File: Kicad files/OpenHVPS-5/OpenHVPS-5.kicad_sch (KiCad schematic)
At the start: 86 parts, among them J1 Conn_01x03_Male, Q1 FQT7N10, Q2 BC846A, Q3 MMBT3906, Q4 MMBT3906, U1 MAX6008AEUR+T, U2 74HC14, U3 MAX4162, U4 CD14538BM

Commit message: Updated ground plane changed, capacitor to 47uF
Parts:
- C4: value 100uF -> 47uF
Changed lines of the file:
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@@
   (title_block
     (title "SafePulse")
-    (date "2021-02-20")
+    (date "2021-02-21")
     (rev "1.12")
     (company "SafeCast Team")
@@
       (effects (font (size 1.27 1.27)) (justify left))
     )
-    (property "Value" "100uF" (id 1) (at 105.791 28.448 0)
+    (property "Value" "47uF" (id 1) (at 105.791 28.448 0)
       (effects (font (size 1.27 1.27)) (justify left))
     )
@@
       (effects (font (size 1.27 1.27)) hide)
     )
-    (property "Datasheet" "https://www.digikey.com/en/products/detail/cal-chip-electronics-inc/GMC21X5R107M6R3NT/12140431" (id 3) (at 102.87 27.305 0)
+    (property "Datasheet" "https://www.digikey.com/en/products/detail/taiyo-yuden/EMK316BBJ476ML-T/7067010" (id 3) (at 102.87 27.305 0)
       (effects (font (size 1.27 1.27)) hide)
     )
@@
       (effects (font (size 1.27 1.27)) hide)
     )
-    (property "Datasheet" "https://www.digikey.com/en/products/detail/bourns-inc/MH2029-221Y/3767626" (id 3) (at 81.28 28.575 0)
+    (property "Datasheet" "https://www.digikey.com/en/products/detail/tdk-corporation/MPZ2012S331ATD25/5040330" (id 3) (at 81.28 28.575 0)
       (effects (font (size 1.27 1.27)) hide)
     )
@@
       (effects (font (size 1.27 1.27)) hide)
     )
-    (property "Datasheet" "https://www.digikey.com/en/products/detail/bourns-inc/MH2029-221Y/3767626" (id 3) (at 115.57 29.845 0)
+    (property "Datasheet" "https://www.digikey.com/en/products/detail/tdk-corporation/MPZ2012S331ATD25/5040330" (id 3) (at 115.57 29.845 0)
       (effects (font (size 1.27 1.27)) hide)
     )
@@
     )
     (path "/00000000-0000-0000-0000-000060023647"
-      (reference "C4") (unit 1) (value "100uF") (footprint "Capacitor_SMD:C_1210_3225Metric")
+      (reference "C4") (unit 1) (value "47uF") (footprint "Capacitor_SMD:C_1210_3225Metric")
     )
     (path "/00000000-0000-0000-0000-0000600248db"

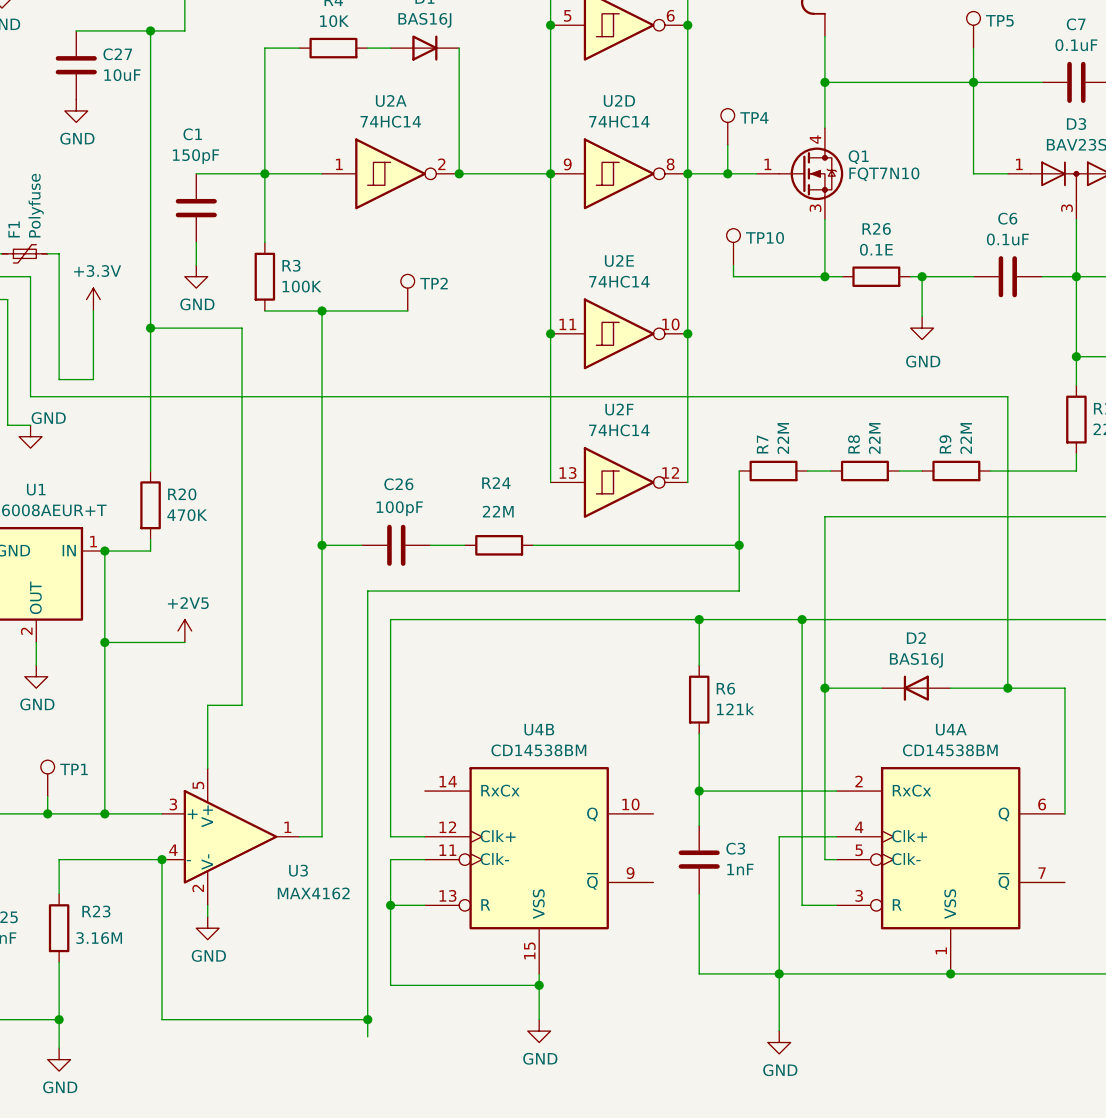
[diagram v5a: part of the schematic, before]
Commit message: added digikey bom from Allan and move U4 label
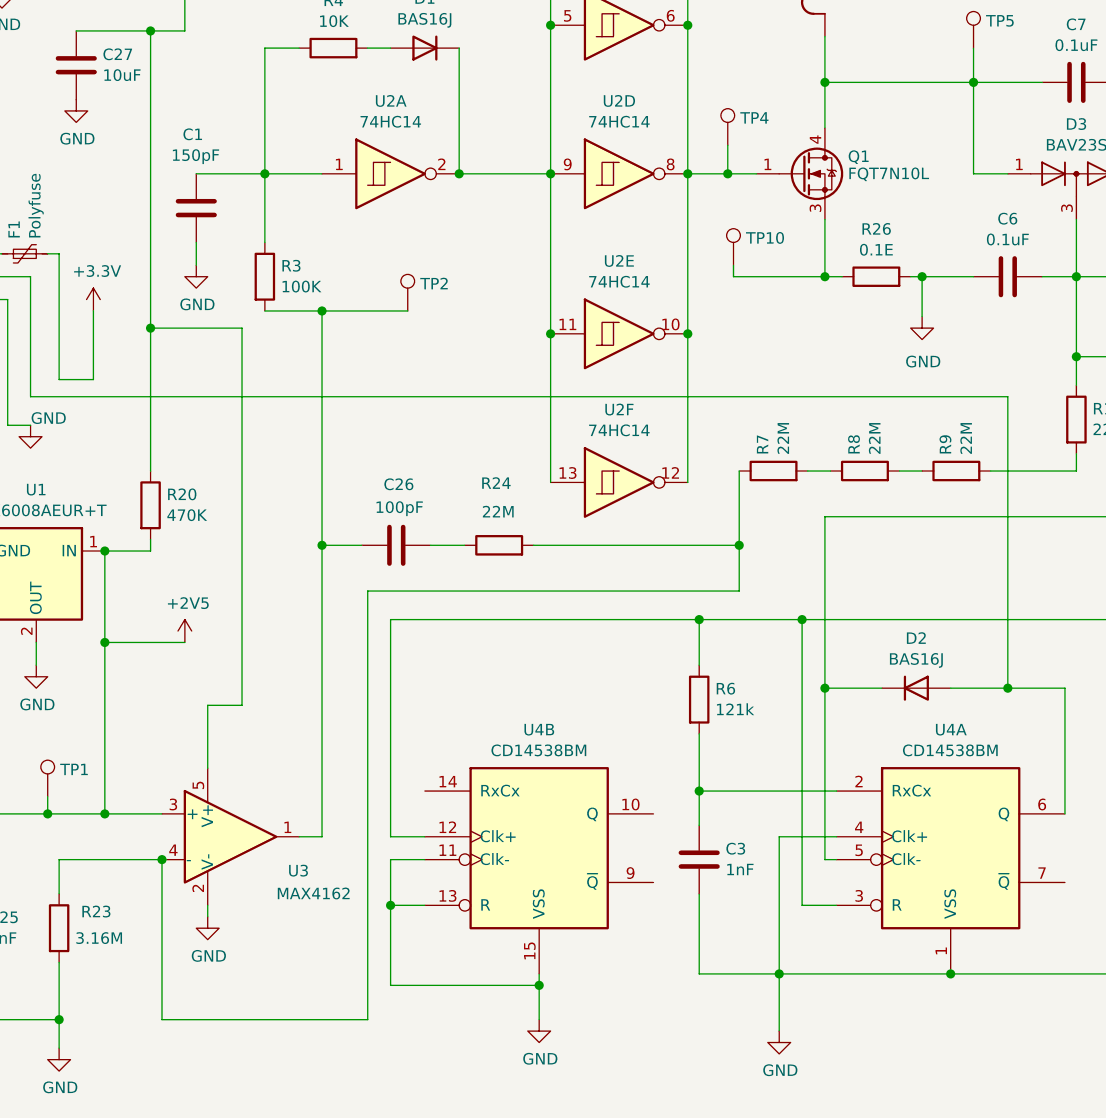
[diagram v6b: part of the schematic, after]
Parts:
- Q1: value FQT7N10 -> FQT7N10L
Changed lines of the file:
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@@
   (title_block
     (title "SafePulse")
-    (date "2021-02-21")
+    (date "2021-02-24")
     (rev "1.12")
     (company "SafeCast Team")
@@
   (junction (at 59.69 103.505) (diameter 1.016) (color 0 0 0 0))
   (junction (at 59.69 129.54) (diameter 1.016) (color 0 0 0 0))
-  (junction (at 64.77 182.245) (diameter 1.016) (color 0 0 0 0))
   (junction (at 67.31 169.545) (diameter 1.016) (color 0 0 0 0))
   (junction (at 74.93 88.265) (diameter 1.016) (color 0 0 0 0))
@@
     (stroke (width 0) (type solid) (color 0 0 0 0))
   )
+  (wire (pts (xy 41.91 182.245) (xy 64.77 182.245))
+    (stroke (width 0) (type solid) (color 0 0 0 0))
+  )
   (wire (pts (xy 44.45 72.39) (xy 44.45 62.23))
     (stroke (width 0) (type solid) (color 0 0 0 0))
@@
     (stroke (width 0) (type solid) (color 0 0 0 0))
   )
-  (wire (pts (xy 64.77 134.62) (xy 64.77 182.245))
-    (stroke (width 0) (type solid) (color 0 0 0 0))
-  )
   (wire (pts (xy 64.77 134.62) (xy 106.045 134.62))
     (stroke (width 0) (type solid) (color 0 0 0 0))
   )
-  (wire (pts (xy 64.77 182.245) (xy 41.91 182.245))
-    (stroke (width 0) (type solid) (color 0 0 0 0))
-  )
-  (wire (pts (xy 64.77 182.245) (xy 64.77 184.15))
+  (wire (pts (xy 64.77 182.245) (xy 64.77 134.62))
     (stroke (width 0) (type solid) (color 0 0 0 0))
   )
@@
       (effects (font (size 1.27 1.27)) (justify left) hide)
     )
-    (property "Datasheet" "https://www.digikey.com/en/products/detail/murata-electronics/PRG21BC0R2MM1RA/966726" (id 3) (at 26.67 97.155 0)
+    (property "Datasheet" "https://www.digikey.com/en/products/detail/murata-electronics/PRG21BC0R6MM1RA/2595395?s=N4IgTCBcDaICwE4AMBaAHAVgIyqygcgCIgC6AvkA" (id 3) (at 26.67 97.155 0)
       (effects (font (size 1.27 1.27)) hide)
     )
@@
       (effects (font (size 1.27 1.27)) hide)
     )
-    (property "Datasheet" "https://www.digikey.com/en/products/detail/panasonic-electronic-components/ERJ-6ENF2002V/111532" (id 3) (at 263.525 144.145 0)
+    (property "Datasheet" "https://www.digikey.com/en/products/detail/stackpole-electronics-inc/RMCF0805FT20K0/1760314" (id 3) (at 263.525 144.145 0)
       (effects (font (size 1.27 1.27)) hide)
     )
@@
       (effects (font (size 1.27 1.27)) (justify left))
     )
-    (property "Value" "FQT7N10" (id 1) (at 118.11 88.265 0)
+    (property "Value" "FQT7N10L" (id 1) (at 118.11 88.265 0)
       (effects (font (size 1.27 1.27)) (justify left))
     )
@@
       (effects (font (size 1.27 1.27) italic) hide)
     )
-    (property "Datasheet" "https://www.infineon.com/dgdl/irf6655pbf.pdf?fileId=5546d462533600a4015355ec76961a5b" (id 3) (at 113.03 88.265 0)
+    (property "Datasheet" "https://www.digikey.com/en/products/detail/on-semiconductor/FQT7N10LTF/965354" (id 3) (at 113.03 88.265 0)
       (effects (font (size 1.27 1.27)) (justify left) hide)
     )
@@
       (effects (font (size 1.27 1.27)) (justify left) hide)
     )
-    (property "Datasheet" "https://www.digikey.com/en/products/detail/maxim-integrated/MAX4162EUK-T/470825" (id 3) (at 49.53 156.845 0)
+    (property "Datasheet" "https://www.digikey.com/en/products/detail/maxim-integrated/MAX4162EUK-T/774077" (id 3) (at 49.53 156.845 0)
       (effects (font (size 1.27 1.27)) hide)
     )
@@
     )
     (path "/0b3e807e-2e2e-4d01-9bff-0d612d23cbec"
-      (reference "Q1") (unit 1) (value "FQT7N10") (footprint "Package_TO_SOT_SMD:SOT-223-3_TabPin4")
+      (reference "Q1") (unit 1) (value "FQT7N10L") (footprint "Package_TO_SOT_SMD:SOT-223-3_TabPin4")
     )
     (path "/00000000-0000-0000-0000-000060126f57"

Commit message: Test
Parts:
- C1: manf# (none) -> test
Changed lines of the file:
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@@
+      (effects (font (size 1.27 1.27)) hide)
+    )
+    (property "manf#" "test" (id 4) (at 45.72 92.075 0)
       (effects (font (size 1.27 1.27)) hide)
     )

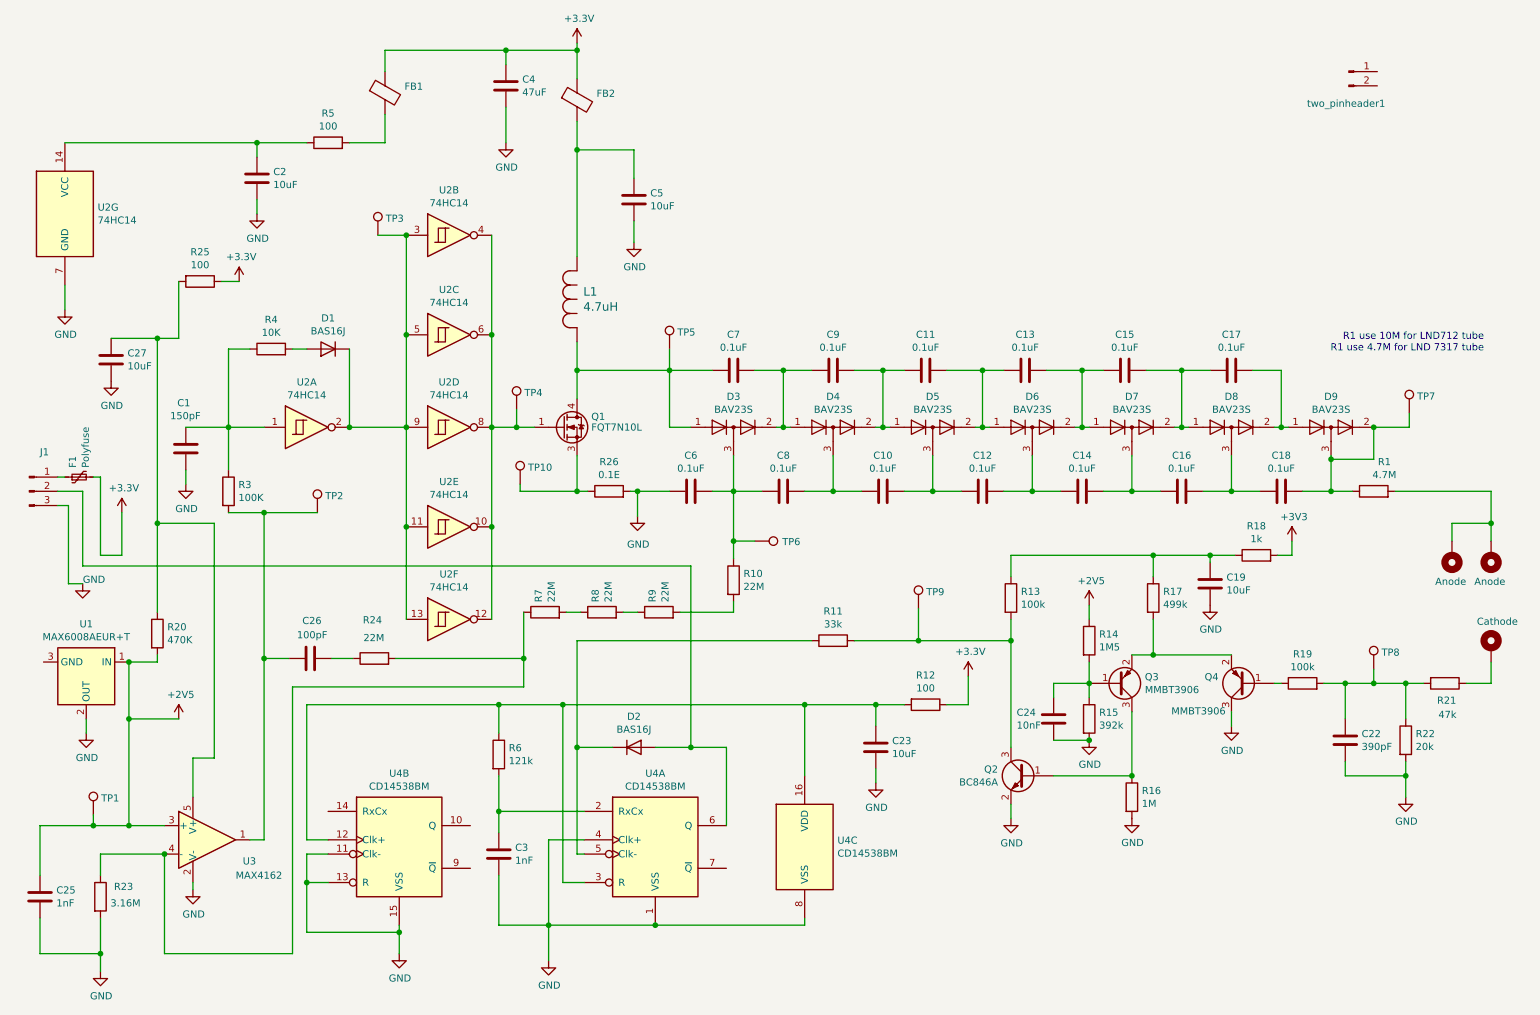
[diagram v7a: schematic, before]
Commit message: Cahged pin sof U3 Max4162. V1.20.0
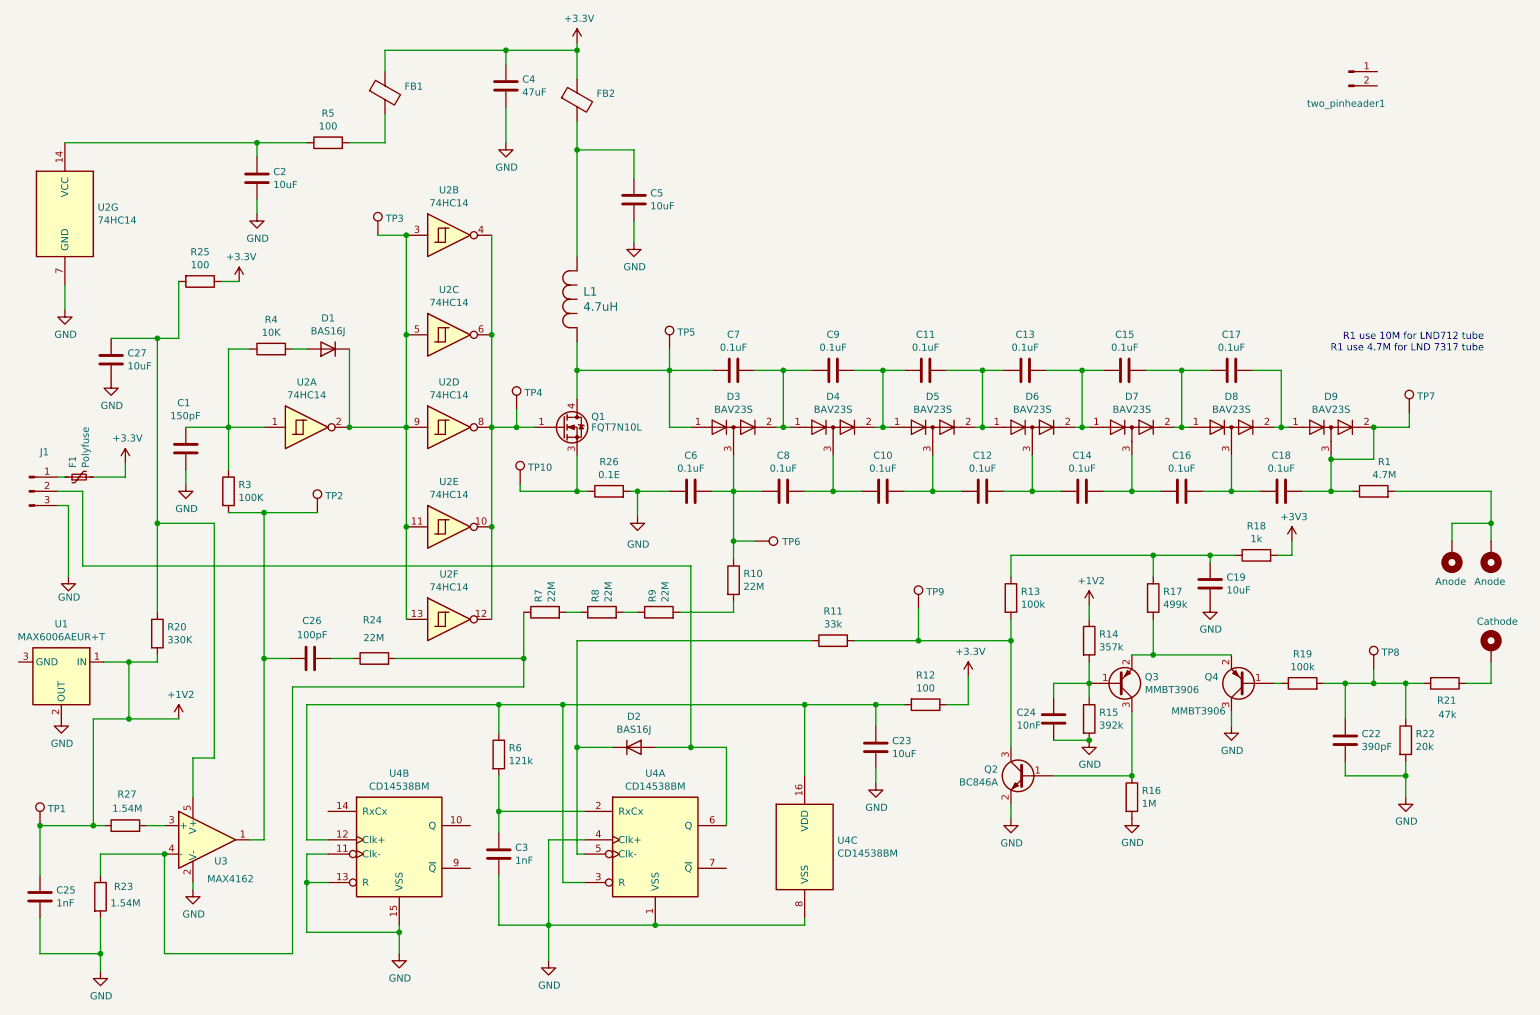
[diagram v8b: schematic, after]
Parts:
- added R27: 1.54M, Resistor_SMD:R_0805_2012Metric, symbol Device:R
- C1: manf# test -> (none)
- R14: value 1M5 -> 357k; Digikey (none) -> 2019-RK73H2ATTD3573FCT-ND
- R20: value 470K -> 330K; Digikey (none) -> A126361CT-ND
- R23: value 3.16M -> 1.54M; Digikey (none) -> 311-1.54MCRCT-ND
- U1: value MAX6008AEUR+T -> MAX6006AEUR+T; Digikey (none) -> MAX6006AEUR+TCT-ND
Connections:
- net +2V5 renamed +1V2
- net +1V2: now also R27.1; no longer U3.3 (+)
- new net: R27.2, U3.3 (+)
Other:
- moved on the sheet: TP1, U1
